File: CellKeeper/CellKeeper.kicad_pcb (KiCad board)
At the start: 4 copper layers, 260 x 113 mm, 480 parts, among them J1 WJ15EDGRC-3.81-04P-14-00A, J10 3.81P Screw Terminal, J11 USB_C_Receptacle_USB2.0_16P, J12 Conn_02x10_Odd_Even, J14 ZE05H-8DP-2H, J15 WJ15EDGRC-3.81-04P-14-00A, J16 Conn_01x03, J17 OEM HV Sense Connector, J18 7.62mm Pitch Screw Terminal, J19 USB_C_Receptacle_USB2.0_16P, J2 T34008, J20 OEM Connector, J21 3.81P Screw Terminal, J22 Conn_02x10_Odd_Even, J3 Screw_Terminal_01x04, J4 8P8C_LED_Shielded_x2, J5 8P8C_LED_Shielded_x2, J6 S44B-RAD1AK, J7 Screw_Terminal_01x04, J8 Conn_01x03, J9 USB_C_Receptacle_USB2.0_16P, Q1 BSC0805LS, Q2 BSC0805LS, Q3 BSC0805LS, Q4 BSC0805LS, SW1 TS-1187A-B-A-B, SW2 TS-1187A-B-A-B, SW3 TS-1187A-B-A-B, SW4 TS-1187A-B-A-B, U1 UCC27524DR, U10 ISO1050DUB, U11 UCC27524DR, U12 LTV-217-B-G, U13 LTV-217-B-G, U14 RP2354B, U15 F0505S-1WR3, U16 ISO1540, U17 INA228, U18 ADS1115, U19 ADS1115, U20 RP2354B, U21 SP3485EN-L/TR, U22 AM26LV32EIDR, U23 W25Q16JVUXIQ, U24 W25Q16JVUXIQ, U25 TLV1117LV33DCYR, U26 TLV1117LV33DCYR, U3 TPS5430DDAR, U4 F0505S-1WR3, U5 ISO1050DUB, U6 LTV-217-B-G, U7 LTV-217-B-G, U8 LTV-217-B-G, U9 LTV-217-B-G, Y1 ABM8-272-T3, Y2 ABM8-272-T3

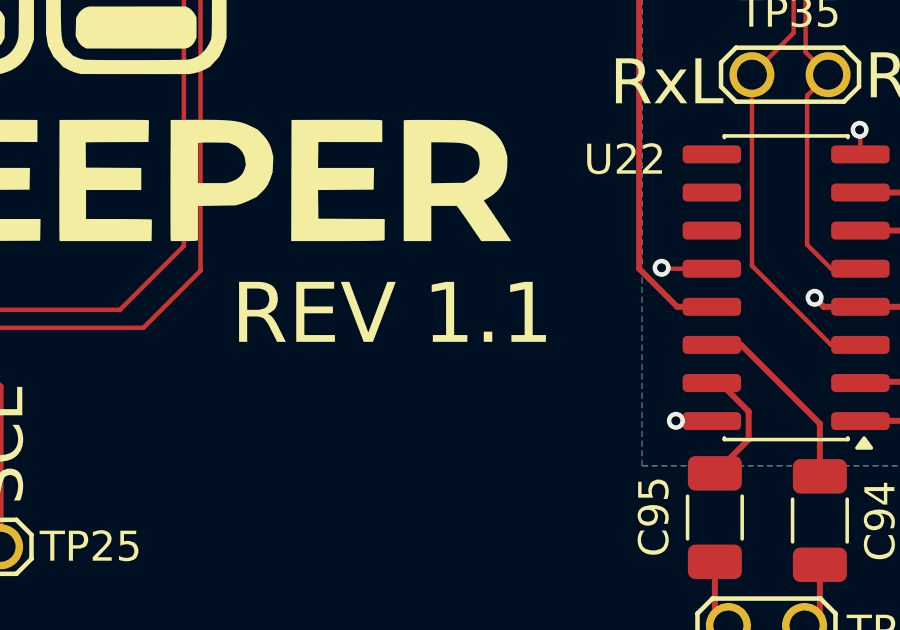
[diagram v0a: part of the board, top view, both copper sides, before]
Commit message: Start rev 1.2: title blocks, silkscreen REV text and fab output name
The REV text's cached glyphs are dropped so KiCad renders 1.2 from the embedded Roboto.
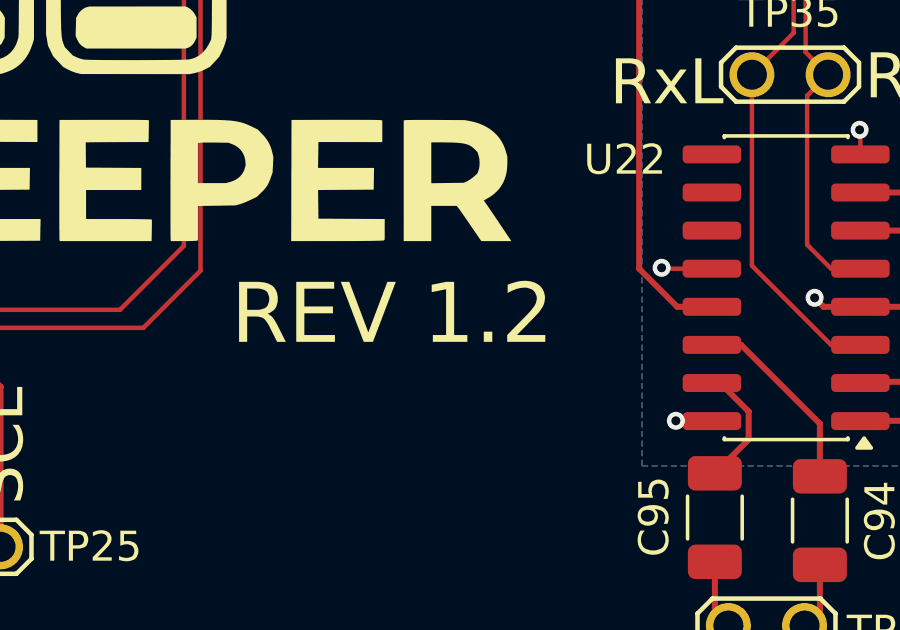
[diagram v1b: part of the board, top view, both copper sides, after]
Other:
- board text added: "REV 1.2"
- board text removed: "REV 1.1"
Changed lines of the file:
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@@
 		(title "CellKeeper")
 		(date "2026-10-26")
-		(rev "1.1")
+		(rev "1.2")
 	)
 	(layers
@@
 		)
 	)
-	(gr_text "REV 1.1"
+	(gr_text "REV 1.2"
 		(at 219.042443 117.212982 0)
 		(layer "F.SilkS")
@@
 			(justify left bottom)
 		)
-		(render_cache "REV 1.1" 0
-			(polygon
-				(pts
-					(xy 219.273374 114.87996) (xy 219.931853 114.87996) (xy 220.08021 114.888362) (xy 220.205393 114.91189)
-					(xy 220.310918 114.948592) (xy 220.407561 115.002527) (xy 220.48562 115.069711) (xy 220.547345 115.150947)
-					(xy 220.591286 115.243383) (xy 220.618907 115.351766) (xy 220.628678 115.479454) (xy 220.614555 115.612021)
-					(xy 220.573357 115.729925) (xy 220.506371 115.834094) (xy 220.414843 115.9219) (xy 220.30364 115.989713)
-					(xy 220.16828 116.039259) (xy 220.094396 116.067957) (xy 219.475485 116.067957) (xy 219.472798 115.853512)
-					(xy 219.940035 115.853512) (xy 220.074548 115.840024) (xy 220.176462 115.80332) (xy 220.259894 115.743613)
-					(xy 220.318489 115.667887) (xy 220.354233 115.578786) (xy 220.366361 115.479454) (xy 220.354588 115.369149)
-					(xy 220.321176 115.277465) (xy 220.285935 115.224623) (xy 220.239323 115.180121) (xy 220.179759 115.143376)
-					(xy 220.075233 115.108843) (xy 219.931853 115.095871) (xy 219.537034 115.095871) (xy 219.537034 116.872982)
-					(xy 219.273374 116.872982)
-				)
-			)
-			(polygon
-				(pts
-					(xy 220.43597 116.872982) (xy 219.952369 115.972336) (xy 220.22702 115.970993) (xy 220.71746 116.856617)
-					(xy 220.71746 116.872982)
-				)
-			)
-			(polygon
-				(pts
-					(xy 222.262418 116.658536) (xy 222.262418 116.872982) (xy 221.209121 116.872982) (xy 221.209121 116.658536)
-				)
-			)
-			(polygon
-				(pts
-					(xy 221.262366 114.87996) (xy 221.262366 116.872982) (xy 220.998706 116.872982) (xy 220.998706 114.87996)
-				)
-			)
-			(polygon
-				(pts
-					(xy 222.123078 115.736153) (xy 222.123078 115.950721) (xy 221.209121 115.950721) (xy 221.209121 115.736153)
-				)
-			)
-			(polygon
-				(pts
-					(xy 222.24874 114.87996) (xy 222.24874 115.095871) (xy 221.209121 115.095871) (xy 221.209121 114.87996)
-				)
-			)
-			(polygon
-				(pts
-					(xy 223.231329 116.570487) (xy 223.81739 114.87996) (xy 224.10291 114.87996) (xy 223.366518 116.872982)
-					(xy 223.162941 116.872982)
-				)
-			)
-			(polygon
-				(pts
-					(xy 222.683493 114.87996) (xy 223.264058 116.570487) (xy 223.336476 116.872982) (xy 223.1329 116.872982)
-					(xy 222.397851 114.87996)
-				)
-			)
-			(polygon
-				(pts
-					(xy 225.829951 114.87996) (xy 225.829951 116.872982) (xy 225.57716 116.872982) (xy 225.57716 115.194423)
-					(xy 225.067547 115.379559) (xy 225.067547 115.152291) (xy 225.790262 114.87996)
-				)
-			)
-			(polygon
-				(pts
-					(xy 226.60359 116.750127) (xy 226.613846 116.690384) (xy 226.643891 116.641561) (xy 226.691386 116.608949)
-					(xy 226.760761 116.597109) (xy 226.83003 116.608945) (xy 226.877509 116.641561) (xy 226.907553 116.690384)
-					(xy 226.917809 116.750127) (xy 226.907594 116.808504) (xy 226.877509 116.856617) (xy 226.830097 116.88867)
-					(xy 226.760761 116.900337) (xy 226.691318 116.888665) (xy 226.643891 116.856617) (xy 226.613806 116.808504)
-				)
-			)
-			(polygon
-				(pts
-					(xy 228.139512 114.87996) (xy 228.139512 116.872982) (xy 227.88672 116.872982) (xy 227.88672 115.194423)
-					(xy 227.377108 115.379559) (xy 227.377108 115.152291) (xy 228.099822 114.87996)
-				)
-			)
-		)
 	)
